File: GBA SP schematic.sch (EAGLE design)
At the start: 187 parts, among them IC2 FT230XQ, J1 DNP, J11 Debug USB, J12 FPC_14, J13 DNP, J14 FPC_14, J2 MICRO_USB, J4 DNP, J5 DNP, J6 FPC_14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

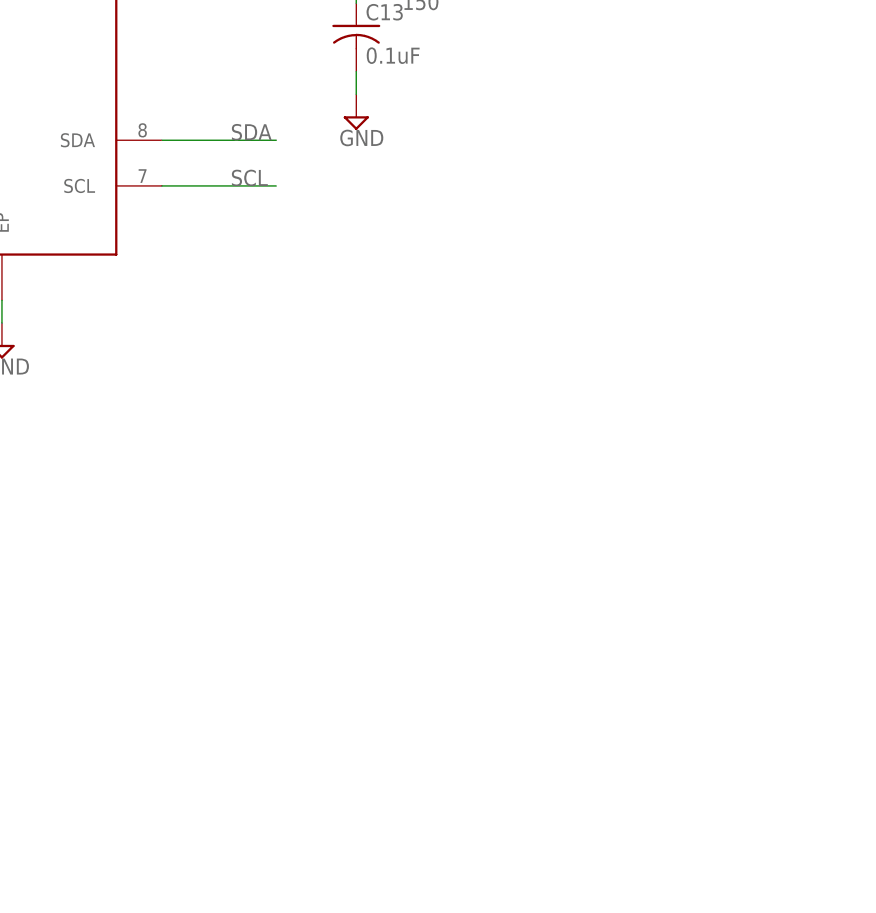
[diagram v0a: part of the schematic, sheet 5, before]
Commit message: Pull-up for battery monitor
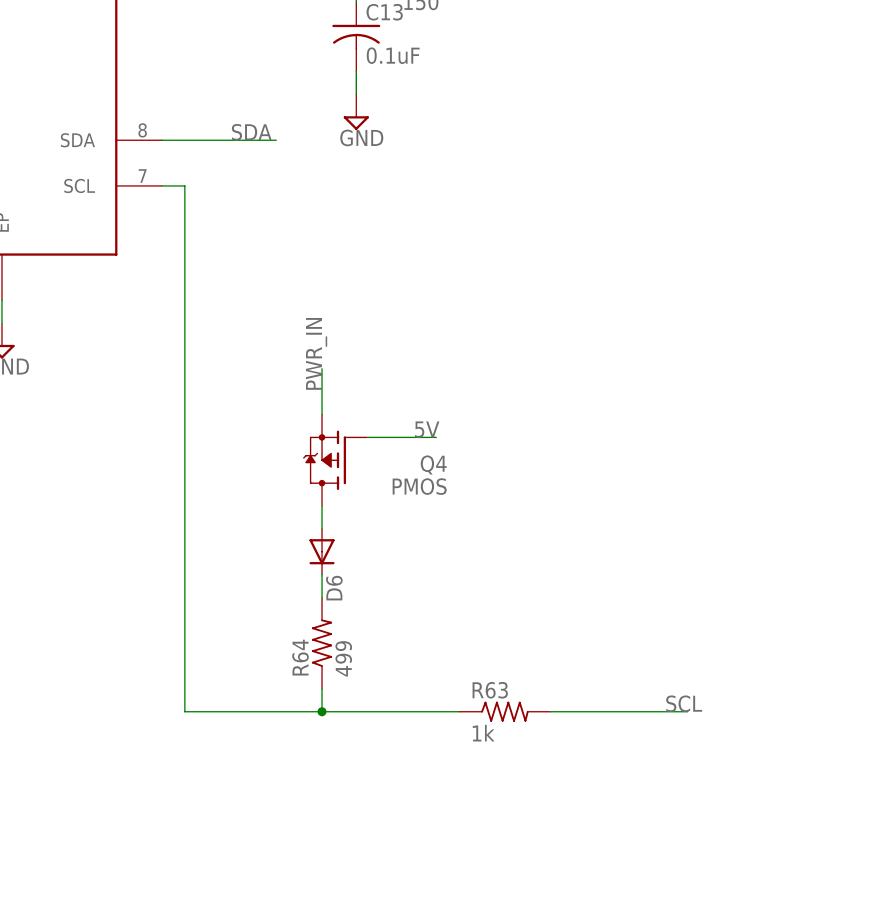
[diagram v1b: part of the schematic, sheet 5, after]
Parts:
- added D6: (no value), diode:DIODE-SOD523
- added Q4: PMOS, Custom_Library:PMOS
- added R63: 1k, rcl:R-US_0402_REAL
- added R64: 499, rcl:R-US_0402_REAL
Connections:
- new net N$32: D6.C, R64.2
- new net N$40: D6.A, Q4.D
- new net N$99: R63.1, R64.1, U8.SCL
- net 5V: now also Q4.G
- net PWR_IN: now also Q4.S
- net SCL: now also R63.2; no longer U8.SCL
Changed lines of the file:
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@@
 <attribute name="MPN" value="CSS-1210TB"/>
 </part>
+<part name="R63" library="rcl" deviceset="R-US_" device="0402_REAL" value="1k"/>
+<part name="Q4" library="Custom_Library" deviceset="PMOS" device=""/>
+<part name="D6" library="diode" deviceset="DIODE-" device="SOD523"/>
+<part name="R64" library="rcl" deviceset="R-US_" device="0402_REAL" value="499"/>
 </parts>
 <sheets>
@@
 <attribute name="VALUE" x="44.958" y="181.61" size="1.778" layer="96" rot="R270"/>
 </instance>
+<instance part="R63" gate="G$1" x="127" y="106.68"/>
+<instance part="Q4" gate="G$1" x="106.68" y="134.62" rot="MR0"/>
+<instance part="D6" gate="G$1" x="106.68" y="124.46" rot="R270"/>
+<instance part="R64" gate="G$1" x="106.68" y="114.3" rot="R90"/>
 </instances>
 <busses>
@@
 <net name="SCL" class="0">
 <segment>
-<pinref part="U8" gate="G$1" pin="SCL"/>
-<wire x1="88.9" y1="165.1" x2="101.6" y2="165.1" width="0.1524" layer="91"/>
-<label x="96.52" y="165.1" size="1.778" layer="95"/>
+<pinref part="R63" gate="G$1" pin="2"/>
+<wire x1="132.08" y1="106.68" x2="147.32" y2="106.68" width="0.1524" layer="91"/>
+<label x="144.78" y="106.68" size="1.778" layer="95"/>
 </segment>
 </net>
@@
 <label x="209.55" y="114.3" size="1.778" layer="95"/>
 </segment>
+<segment>
+<pinref part="Q4" gate="G$1" pin="G"/>
+<wire x1="111.76" y1="137.16" x2="119.38" y2="137.16" width="0.1524" layer="91"/>
+<label x="116.84" y="137.16" size="1.778" layer="95"/>
+</segment>
 </net>
 <net name="PGD" class="0">
@@
 </segment>
 </net>
+<net name="N$99" class="0">
+<segment>
+<pinref part="U8" gate="G$1" pin="SCL"/>
+<wire x1="88.9" y1="165.1" x2="91.44" y2="165.1" width="0.1524" layer="91"/>
+<pinref part="R63" gate="G$1" pin="1"/>
+<wire x1="121.92" y1="106.68" x2="106.68" y2="106.68" width="0.1524" layer="91"/>
+<wire x1="106.68" y1="106.68" x2="91.44" y2="106.68" width="0.1524" layer="91"/>
+<wire x1="91.44" y1="106.68" x2="91.44" y2="165.1" width="0.1524" layer="91"/>
+<pinref part="R64" gate="G$1" pin="1"/>
+<wire x1="106.68" y1="109.22" x2="106.68" y2="106.68" width="0.1524" layer="91"/>
+<junction x="106.68" y="106.68"/>
+</segment>
+</net>
+<net name="PWR_IN" class="0">
+<segment>
+<pinref part="Q4" gate="G$1" pin="S"/>
+<wire x1="106.68" y1="139.7" x2="106.68" y2="144.78" width="0.1524" layer="91"/>
+<label x="106.68" y="142.24" size="1.778" layer="95" rot="R90"/>
+</segment>
+</net>
+<net name="N$32" class="0">
+<segment>
+<pinref part="R64" gate="G$1" pin="2"/>
+<pinref part="D6" gate="G$1" pin="C"/>
+<wire x1="106.68" y1="119.38" x2="106.68" y2="121.92" width="0.1524" layer="91"/>
+</segment>
+</net>
+<net name="N$40" class="0">
+<segment>
+<pinref part="D6" gate="G$1" pin="A"/>
+<pinref part="Q4" gate="G$1" pin="D"/>
+<wire x1="106.68" y1="127" x2="106.68" y2="129.54" width="0.1524" layer="91"/>
+</segment>
+</net>
